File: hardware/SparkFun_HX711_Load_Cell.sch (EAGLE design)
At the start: 30 parts, among them Q1 MMBT4403, U1 HX711, U7 OSHW-LOGOS

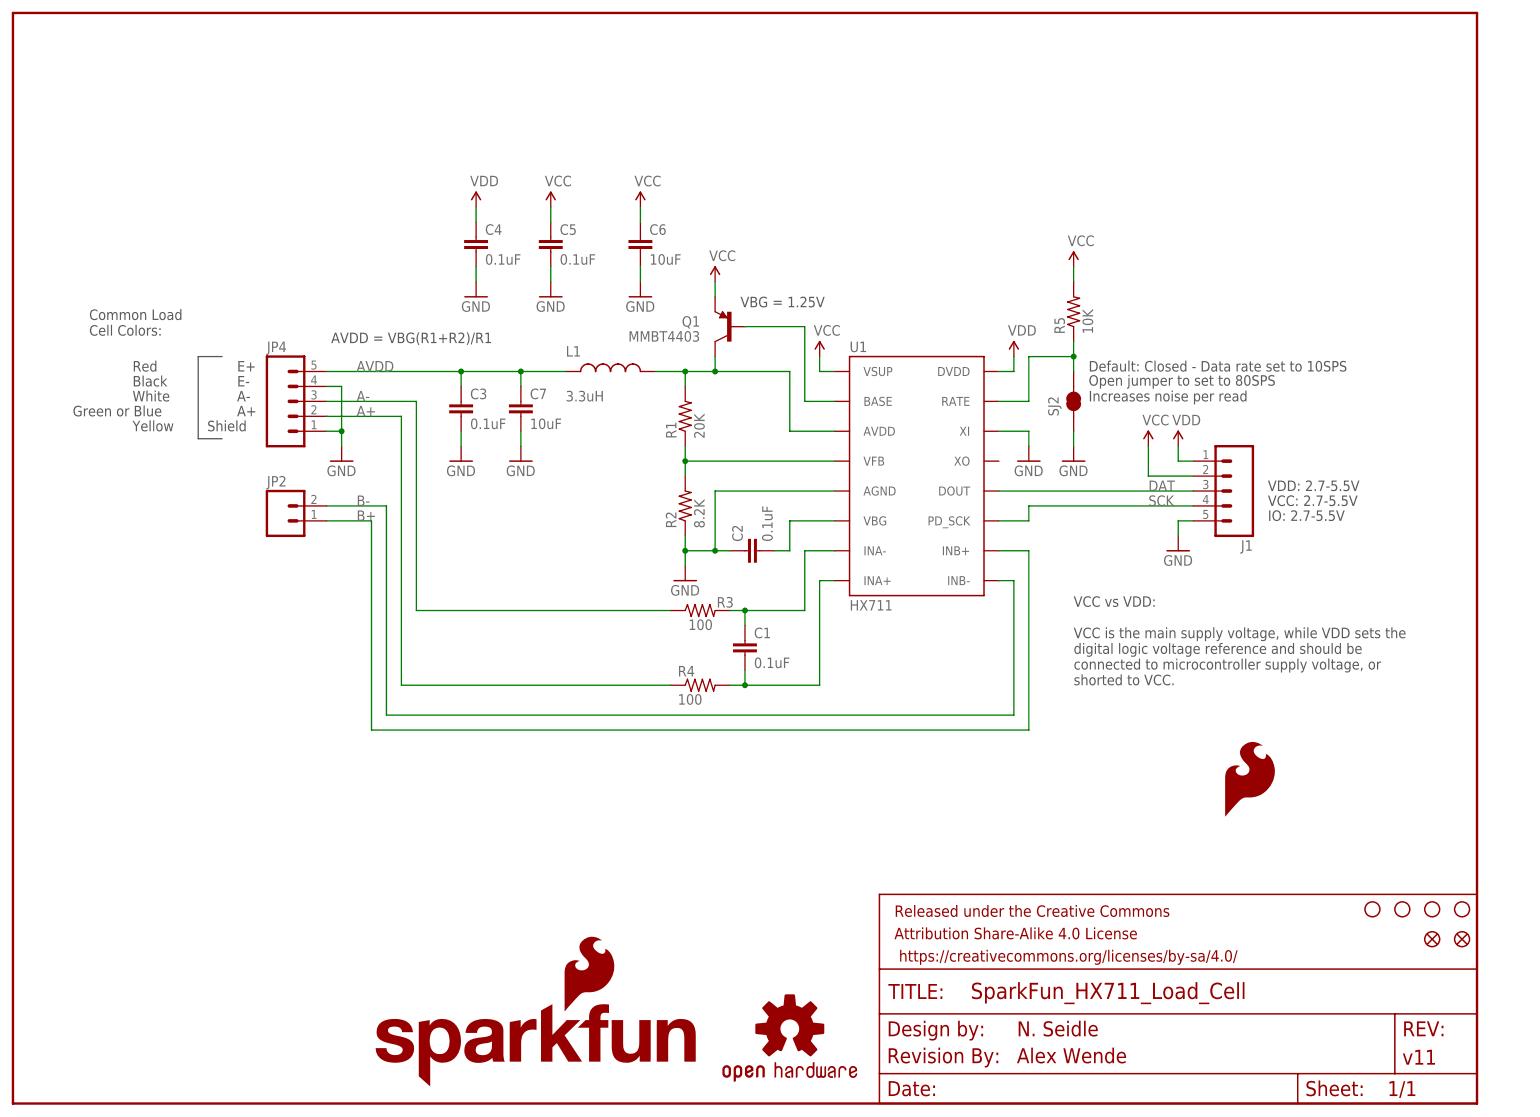
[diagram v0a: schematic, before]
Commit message: V11 Update
Removed spaces from file names
Fixed silk causing CAM errors
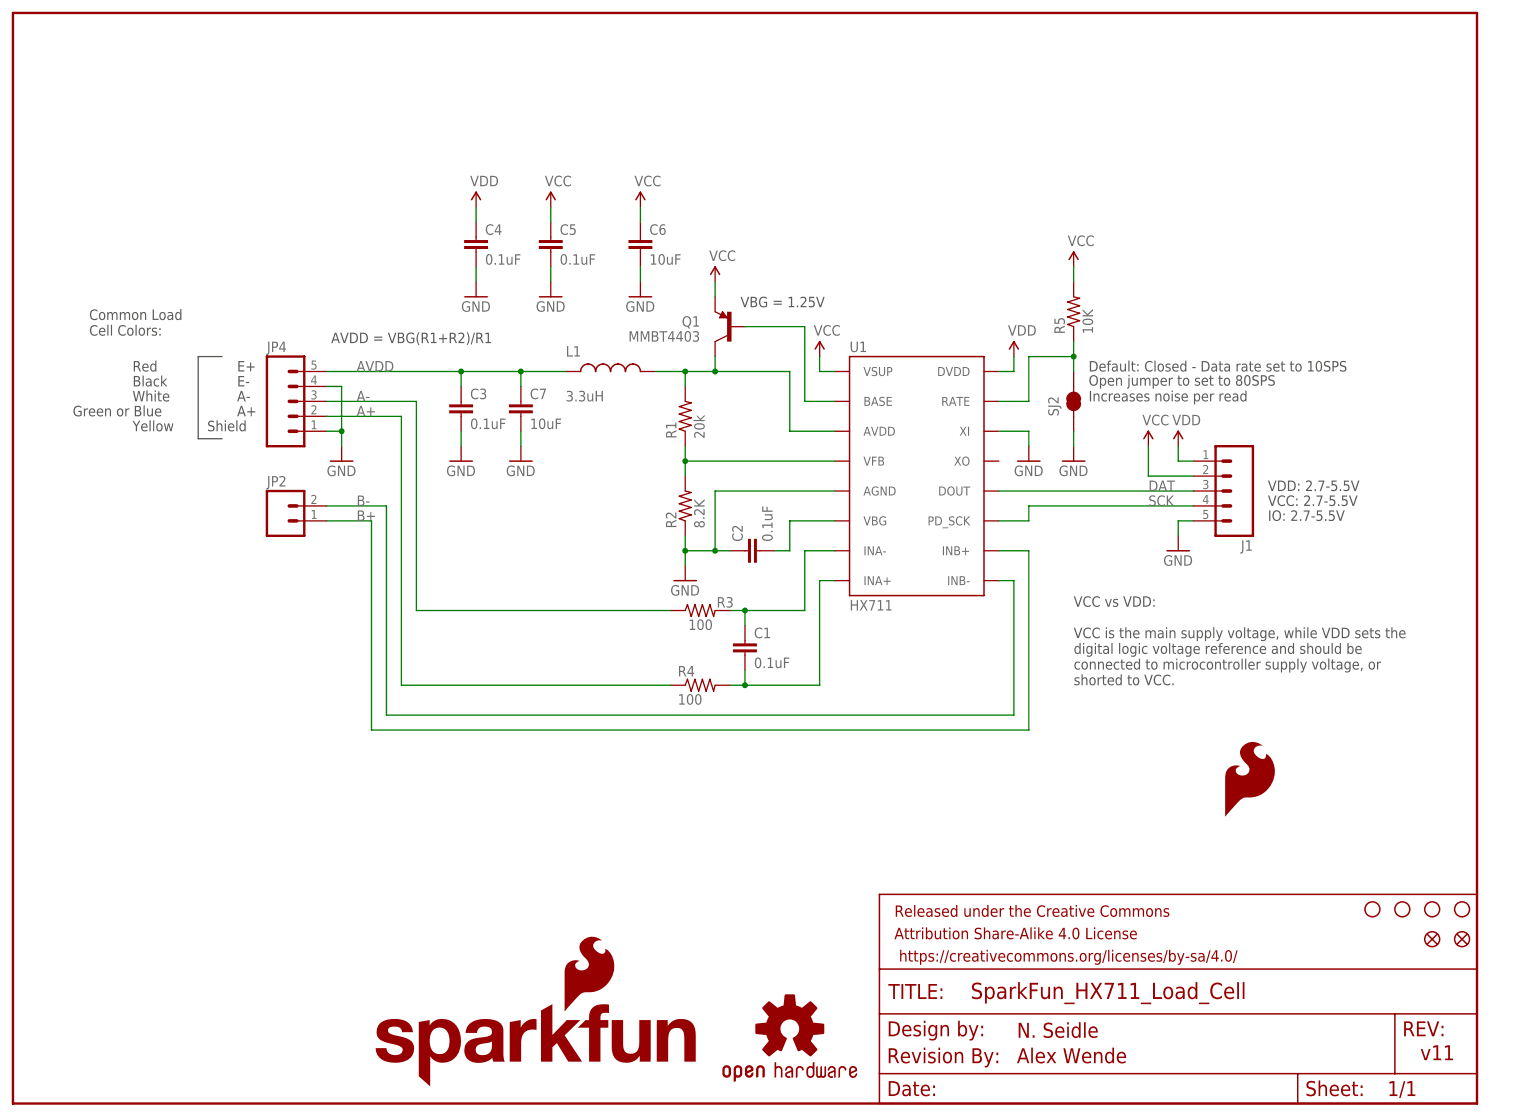
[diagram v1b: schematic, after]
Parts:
- FRAME1: value (none) -> FRAME-LETTER; DESIGNER N. Seidle -> (none); VERSION v11 -> (none)
- JP2: value M02PTH -> (none)
- R1: value 20K -> 20k
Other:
- note added: "N. Seidle"
- note added: "v11"
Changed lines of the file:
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@@
 <part name="GND4" library="SparkFun-Aesthetics" deviceset="GND" device=""/>
 <part name="R2" library="SparkFun-Resistors" deviceset="8.2KOHM-1/10W-5%(0603)" device="" value="8.2K"/>
-<part name="R1" library="SparkFun-Resistors" deviceset="20KOHM1/10W1%(0603)" device="" value="20K"/>
+<part name="R1" library="SparkFun-Resistors" deviceset="20KOHM1/10W1%(0603)" device="" value="20k"/>
 <part name="GND5" library="SparkFun-Aesthetics" deviceset="GND" device=""/>
 <part name="SUPPLY5" library="SparkFun-Aesthetics" deviceset="VCC" device=""/>
@@
 <part name="FID1" library="SparkFun-Aesthetics" deviceset="FIDUCIAL" device="1X2"/>
 <part name="FID2" library="SparkFun-Aesthetics" deviceset="FIDUCIAL" device="1X2"/>
-<part name="JP2" library="SparkFun-Connectors" deviceset="M02" device="PTH" value=""/>
+<part name="JP2" library="SparkFun-Connectors" deviceset="M02" device="PTH"/>
 <part name="SJ2" library="SparkFun-Passives" deviceset="JUMPER-PAD-2-NC_BY_TRACE" device="" value=""/>
 <part name="JP4" library="SparkFun-Connectors" deviceset="M05" device="PTH"/>
@@
 <part name="GND6" library="SparkFun-Aesthetics" deviceset="GND" device=""/>
 <part name="GND9" library="SparkFun-Aesthetics" deviceset="GND" device=""/>
-<part name="FRAME1" library="SparkFun-Aesthetics" deviceset="FRAME-LETTER" device="">
-<attribute name="DESIGNER" value="N. Seidle"/>
-<attribute name="VERSION" value="v11"/>
-</part>
+<part name="FRAME1" library="SparkFun-Aesthetics" deviceset="FRAME-LETTER" device=""/>
 <part name="J1" library="SparkFun-Connectors" deviceset="M05" device="PTH"/>
 <part name="SUPPLY4" library="SparkFun-Aesthetics" deviceset="VDD" device=""/>
@@
 shorted to VCC.</text>
 <text x="170.688" y="6.858" size="2.54" layer="94">Alex Wende</text>
+<text x="170.688" y="11.176" size="2.54" layer="94">N. Seidle</text>
+<text x="239.268" y="7.366" size="2.54" layer="94">v11</text>
 </plain>
 <instances>

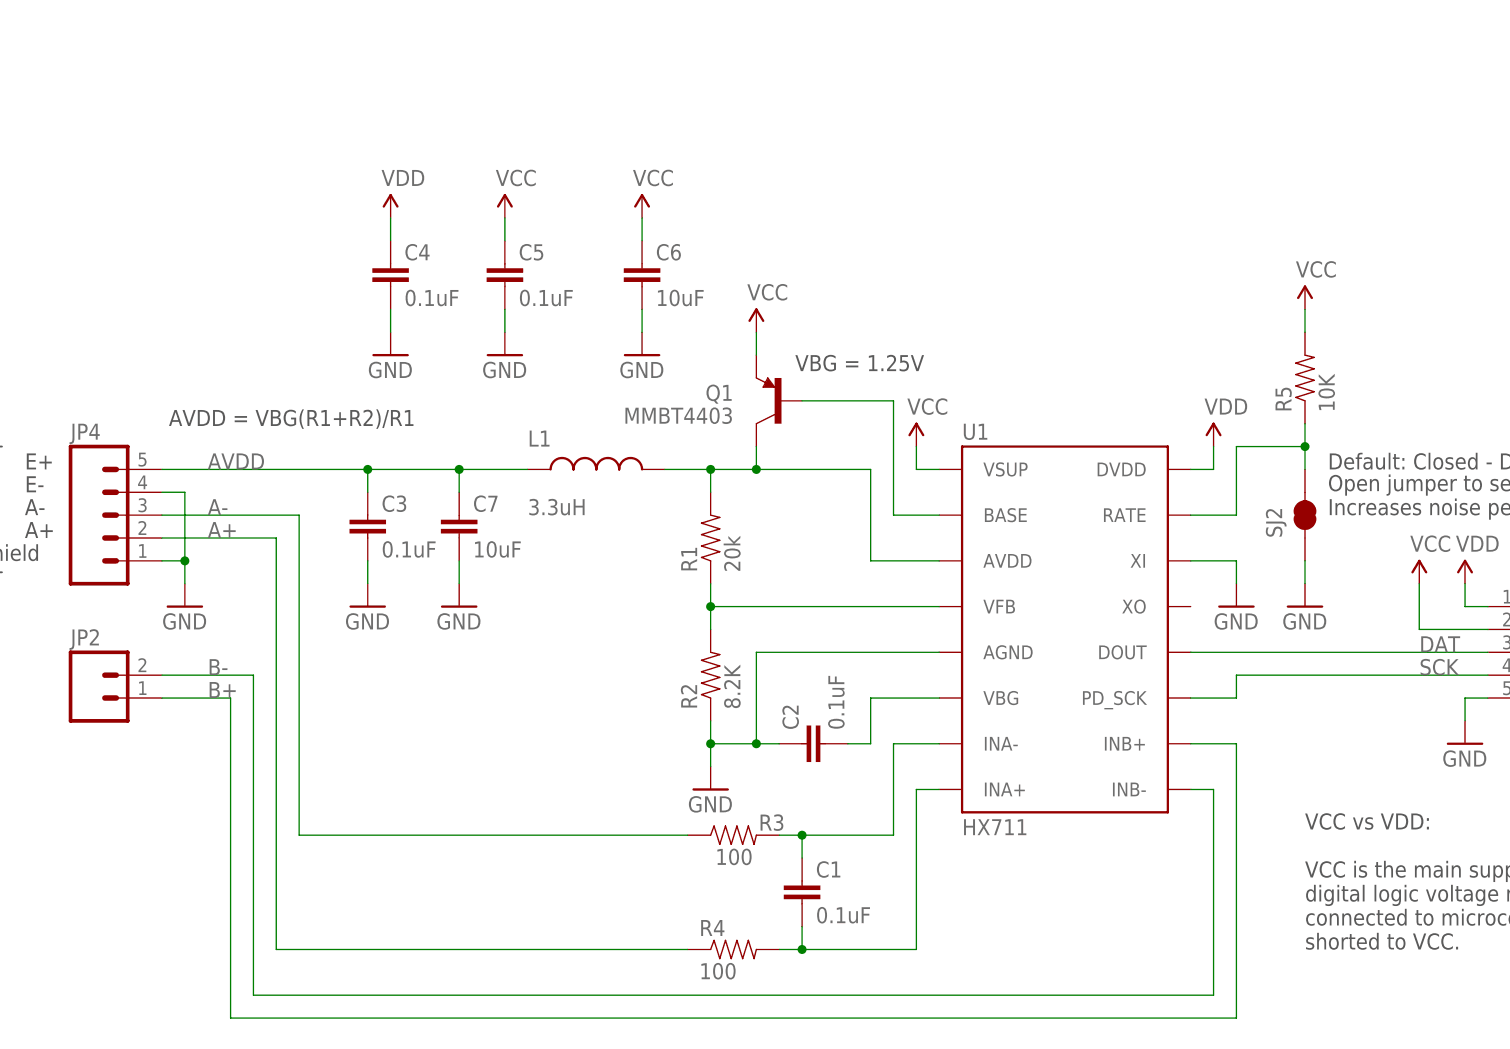
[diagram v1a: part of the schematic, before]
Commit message: Updated Schematic and Datasheet
-Updated to the newest datasheet for the HX711 which corrected the equation from AVDD = VBG(R1+R2)/R1 to AVDD = VBG(R1+R2)/R2.
-Updated the schematic with the correct equation
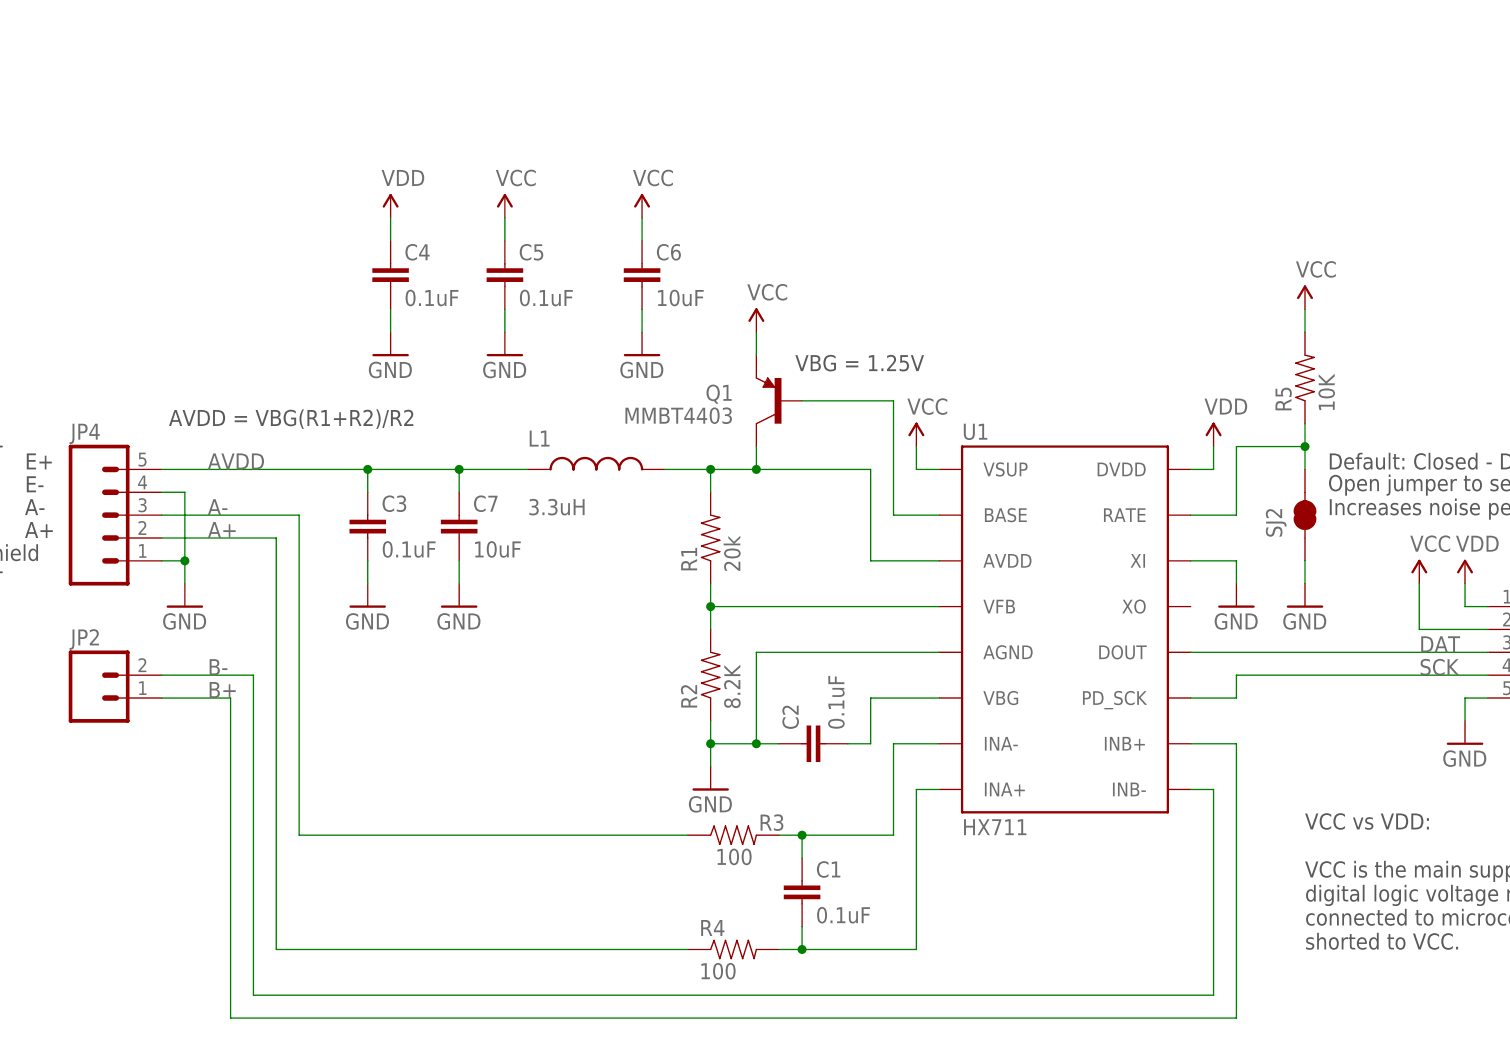
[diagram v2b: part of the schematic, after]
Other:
- note added: "AVDD = VBG(R1+R2)/R2"
- note removed: "AVDD = VBG(R1+R2)/R1"
